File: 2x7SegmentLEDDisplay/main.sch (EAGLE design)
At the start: 21 parts, among them IC1 SCT2167CSSG, IC2 SCT2167CSSG, Q1 BC327, Q2 BC327

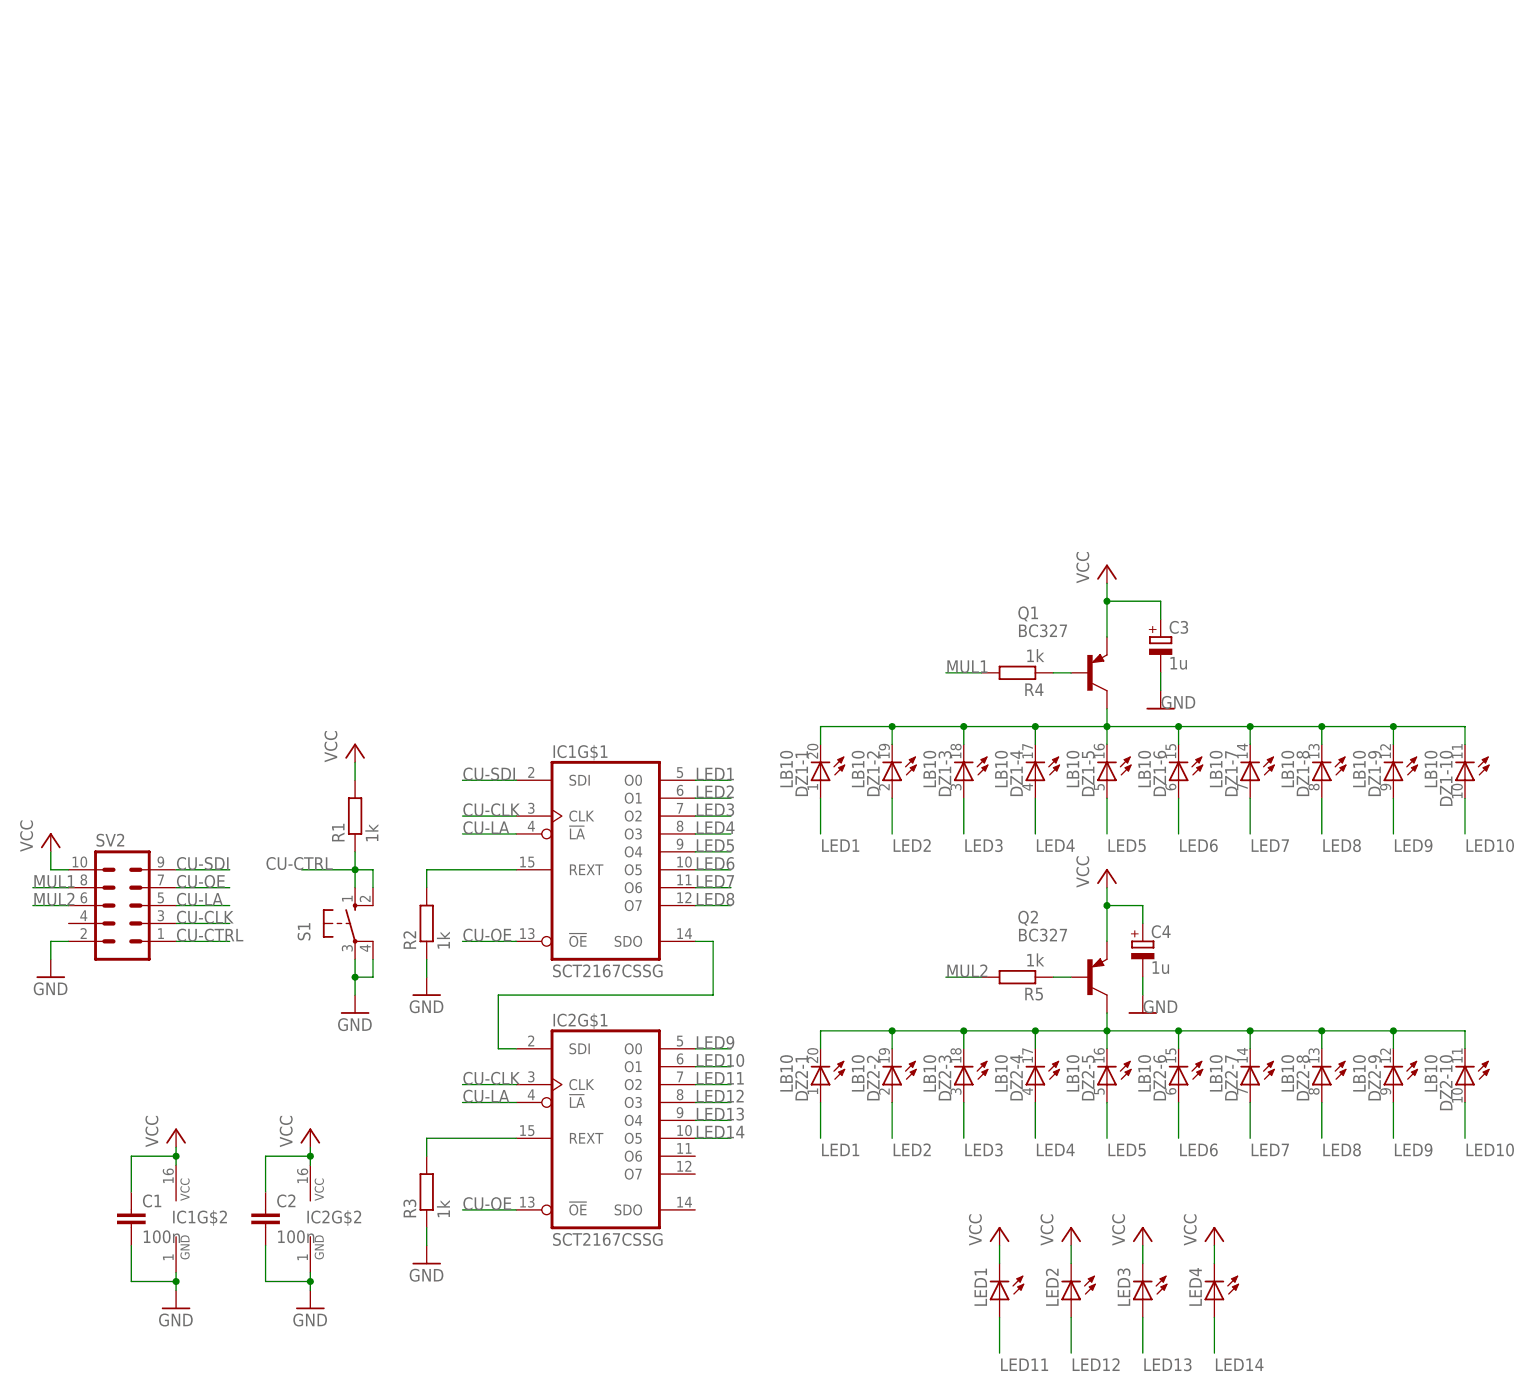
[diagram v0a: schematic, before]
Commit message: 7 Segment LED Display project added.
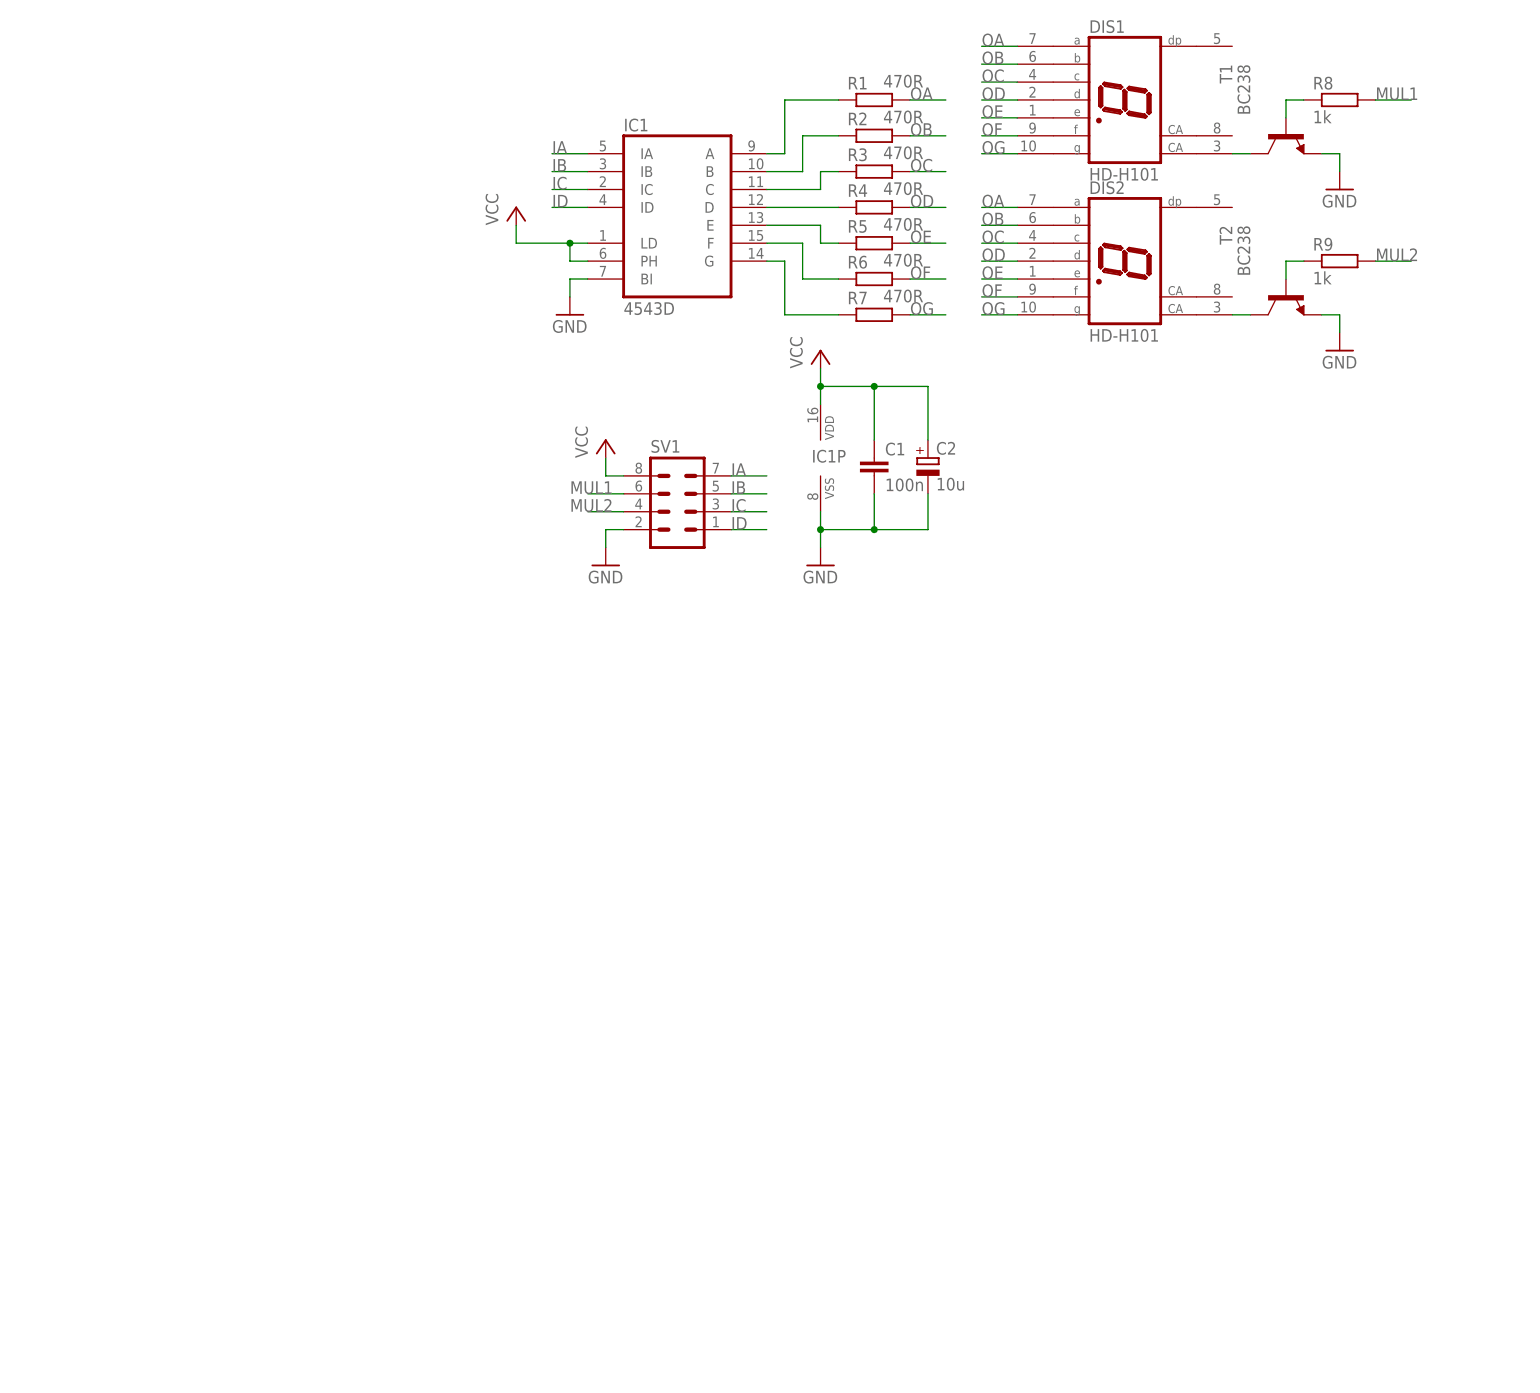
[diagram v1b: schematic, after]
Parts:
- removed C3, C4: 1u, resistor:CPOL-EUSMCA
- removed DZ1, DZ2: LB10, led:LB10
- removed IC2: SCT2167CSSG, starchips:SCT2167CSSG
- removed LED1, LED2, LED3, LED4: (no value), led:LEDSML0603
- removed Q1, Q2: BC327, transistor-pnp:BC327
- removed S1: (no value), switch-omron:10-XX
- removed SV2: (no value), con-lstb:MA05-2
- added DIS1, DIS2: HD-H101, display-hp:HD-H101
- added R6, R7: 470R, resistor:R-EU_R1206
- added R8, R9: 1k, resistor:R-EU_R1206
- added SV1: (no value), con-lstb:MA04-2
- added T1, T2: BC238, transistor:BC238
- C2: value 100n -> 10u; device resistor:C-EUC1206 -> resistor:CPOL-EUSMCA
- IC1: value SCT2167CSSG -> 4543D; device starchips:SCT2167CSSG -> 45xx:4543D
- R1, R2, R3, R4, R5: value 1k -> 470R
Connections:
- removed net CU-CLK: IC1G$1.CLK, IC2G$1.CLK, SV2.3
- removed net CU-CTRL: R1.1, S1.S, S1.S1, SV2.1
- removed net CU-LA: IC1G$1.!LA, IC2G$1.!LA, SV2.5
- removed net CU-OE: IC1G$1.!OE, IC2G$1.!OE, SV2.7
- removed net CU-SDI: IC1G$1.SDI, SV2.9
- removed net LED1: DZ1-1.A, DZ2-1.A, IC1G$1.O0
- removed net LED10: DZ1-10.A, DZ2-10.A, IC2G$1.O1
- removed net LED11: IC2G$1.O2, LED1.A
- removed net LED12: IC2G$1.O3, LED2.A
- removed net LED13: IC2G$1.O4, LED3.A
- removed net LED14: IC2G$1.O5, LED4.A
- removed net LED2: DZ1-2.A, DZ2-2.A, IC1G$1.O1
- removed net LED3: DZ1-3.A, DZ2-3.A, IC1G$1.O2
- removed net LED4: DZ1-4.A, DZ2-4.A, IC1G$1.O3
- removed net LED5: DZ1-5.A, DZ2-5.A, IC1G$1.O4
- removed net LED6: DZ1-6.A, DZ2-6.A, IC1G$1.O5
- removed net LED7: DZ1-7.A, DZ2-7.A, IC1G$1.O6
- removed net LED8: DZ1-8.A, DZ2-8.A, IC1G$1.O7
- removed net LED9: DZ1-9.A, DZ2-9.A, IC2G$1.O0
- removed net N$13: IC2G$1.REXT, R3.2
- new net IA: IC1A.IA, SV1.7
- new net IB: IC1A.IB, SV1.5
- new net IC: IC1A.IC, SV1.3
- new net ID: IC1A.ID, SV1.1
- new net N$1: IC1A.D, R4.1
- new net N$10: IC1A.G, R7.1
- new net N$11: R9.1, T2.B
- new net N$14: DIS2.CA, T2.C
- new net N$9: IC1A.A, R1.1
- new net OA: DIS1.A, DIS2.A, R1.2
- new net OB: DIS1.B, DIS2.B, R2.2
- new net OC: DIS1.C, DIS2.C, R3.2
- new net OD: DIS1.D, DIS2.D, R4.2
- new net OE: DIS1.E, DIS2.E, R5.2
- new net OF: DIS1.F, DIS2.F, R6.2
- new net OG: DIS1.G, DIS2.G, R7.2
- net GND: now also C2.-, IC1A.BI, IC1P.VSS, SV1.2, T1.E, T2.E; no longer C2.2, C3.-, C4.-, IC1G$2.GND, IC2G$2.GND, R2.1, R3.1, S1.P, S1.P1, SV2.2
- net MUL1: now also R8.2, SV1.6; no longer R4.2, SV2.8
- net MUL2: now also R9.2, SV1.4; no longer R5.2, SV2.6
- net N$2: now also IC1A.C, R3.1; no longer DZ1-1.C, DZ1-10.C, DZ1-2.C, DZ1-3.C, DZ1-4.C, DZ1-5.C, DZ1-6.C, DZ1-7.C, DZ1-8.C, DZ1-9.C, Q1.C
- net N$3: now also IC1A.B, R2.1; no longer IC1G$1.SDO, IC2G$1.SDI
- net N$4: now also IC1A.E, R5.1; no longer Q1.B, R4.1
- net N$5: now also DIS1.CA, T1.C; no longer DZ2-1.C, DZ2-10.C, DZ2-2.C, DZ2-3.C, DZ2-4.C, DZ2-5.C, DZ2-6.C, DZ2-7.C, DZ2-8.C, DZ2-9.C, Q2.C
- net N$6: now also R8.1, T1.B; no longer Q2.B, R5.1
- net N$8: now also IC1A.F, R6.1; no longer IC1G$1.REXT, R2.2
- net VCC: now also C2.+, IC1A.LD, IC1A.PH, IC1P.VDD, SV1.8; no longer C2.1, C3.+, C4.+, IC1G$2.VCC, IC2G$2.VCC, LED1.C, LED2.C, LED3.C, LED4.C, Q1.E, Q2.E, R1.2, SV2.10
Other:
- moved on the sheet: C1, R1, R2, R3, R4, R5
